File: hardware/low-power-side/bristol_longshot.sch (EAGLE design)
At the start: 68 parts, among them U1 SAM_D20E, U10 ADP1607ACPZN-R7, U11 TPS73118DBVT, U2 SI4060, U3 SE880, U4 SST25WF040BT-40I/NP, U5 TG-5006CJ, U6 TG-5006CJ, U7 TPS3123, U8 SN74LVC1G32DCKR, U9 MS5607-02BA03, Y1 ABS05

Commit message: [low-power-side] More work on board, vaguely complete. Added parts list
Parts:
- removed R10: 100kΩ, microbuilder_v3:RESISTOR_0402
- removed R11: 240kΩ, microbuilder_v3:RESISTOR_0402
- added R2, R3, R4: 10kΩ, microbuilder_v3:RESISTOR_0402
- C10: value 100nF -> 100pF
- C11: value 100nF -> 1nF
- C12: value 1µF -> 10nF
- C20: value 18pF -> 100nF
- C21: value 2.2µF -> 100nF
- C22: value 4.7µF -> 100nF
- C23: value 18pF -> 1µF
- C24: value 1nF -> 1µF
- C25: value 100nF -> 2.2µF
- C26: value 10µF -> 4.7µF; device resistor:C-EUC0603K -> microbuilder_v3:CAP_CERAMIC_0402
- C27, C28: value 10µF -> 18pF; device resistor:C-EUC0603K -> microbuilder_v3:CAP_CERAMIC_0402
- C29: value 1µF -> 10µF; device microbuilder_v3:CAP_CERAMIC_0402 -> resistor:C-EUC0603K
- C30: value 10nF -> 10µF; device microbuilder_v3:CAP_CERAMIC_0402 -> resistor:C-EUC0603K
- C31: value 100µF -> 10µF; device resistor:C-EUC1210K -> resistor:C-EUC0603K
- C32: value 100pF -> 100µF; device microbuilder_v3:CAP_CERAMIC_0402 -> resistor:C-EUC1210K
- R7, R9: value 10kΩ -> 100kΩ
- R8: value 10kΩ -> 43kΩ
- renumbered U$48 to A1
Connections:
- removed net GPS!RESET: U1.PA03
- new net EXT_THERMISTOR_SENSE: R7.2, U1.PA03
- net 1.2V: now also C29.1; no longer C27.1
- net 1.8V: now also C21.P$1, C26.P$1, C30.1, C32.1, R4.2, R8.2; no longer C22.P$1, C26.1, C31.1, C32.P$1, R10.2, R7.2
- net FB: now also R8.1, R9.2; no longer R10.1, R11.2
- net GND: now also C26.P$2, C27.P$2, C28.P$2, C29.2, C30.2, C32.2, R2.1, R3.1, R7.1; no longer C26.2, C27.2, C28.2, C29.P$2, C30.P$2, C32.P$2, R11.1, R8.1
- net RADIO_VDD: now also C20.P$1, C25.P$1; no longer C11.P$1, C21.P$1
- net RTC_XI: now also C27.P$1; no longer C20.P$1
- net RTC_XO: now also C28.P$1; no longer C23.P$1
- net SE_GPIO0: now also R2.2; no longer R9.2
- net SE_GPIO1: now also R3.2; no longer R8.2
- net SE_MODE_PULL: now also R4.1; no longer R7.1
- net TCXO_REG_IN: now also C23.P$1; no longer C29.P$1
- net TCXO_REG_NR: now also C12.P$1; no longer C30.P$1
- net TCXO_VDD: now also C24.P$1; no longer C12.P$1
- net TCXO_VDD1: now also C11.P$1, C22.P$1, C31.1; no longer C24.P$1, C25.P$1, C28.1
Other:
- note added: "Nominal output voltage 1.80V Using 0.1% resistors most of the variablity is in V_FB Specified 1.76V - 1.85V"
- note added: "Si4468 Transciever"
- note removed: "Si4060 Transmitter"
- moved on the sheet: C10, C11, C12, C20, C21, C22, C23, C24, C25, C26, C27, C28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

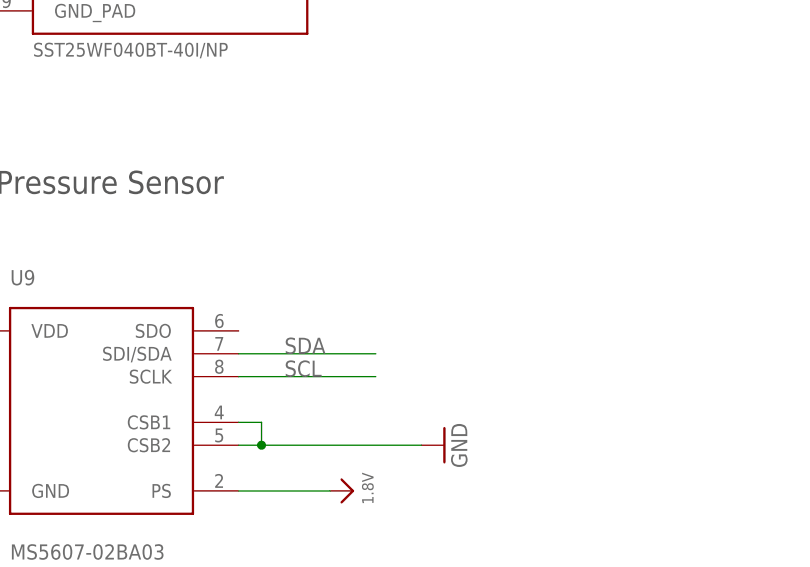
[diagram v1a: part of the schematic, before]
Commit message: [low-power-side] Added 10k i2c pull ups
v0.986.0 -> v0.986.1
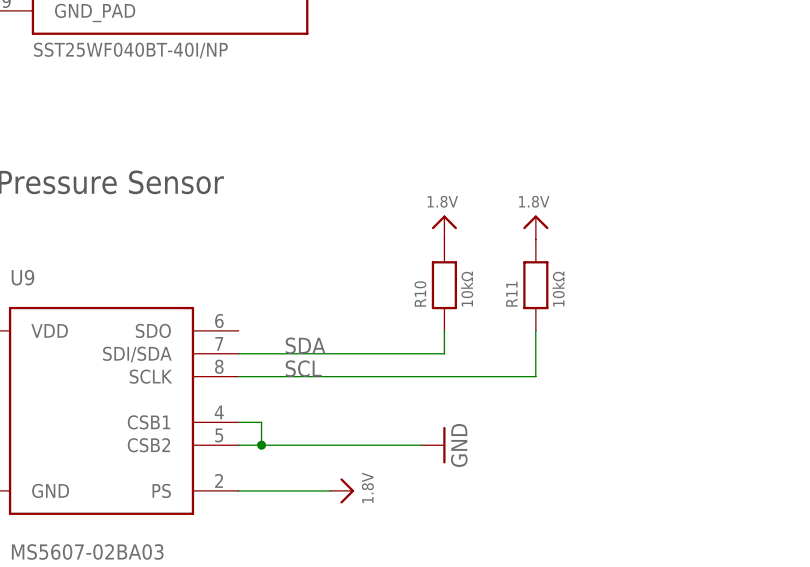
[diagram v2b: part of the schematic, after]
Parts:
- added R10, R11: 10kΩ, microbuilder_v3:RESISTOR_0402
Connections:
- net 1.8V: now also R10.2, R11.2
- net SCL: now also R11.1
- net SDA: now also R10.1
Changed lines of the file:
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@@
 <part name="U$47" library="microbuilder_v3" deviceset="GND" device=""/>
 <part name="U$53" library="microbuilder_v3" deviceset="1.8V" device=""/>
+<part name="R10" library="microbuilder_v3" deviceset="RESISTOR" device="_0402" value="10kΩ"/>
+<part name="R11" library="microbuilder_v3" deviceset="RESISTOR" device="_0402" value="10kΩ"/>
+<part name="U$48" library="microbuilder_v3" deviceset="1.8V" device=""/>
+<part name="U$54" library="microbuilder_v3" deviceset="1.8V" device=""/>
 </parts>
 <sheets>
@@
 <instance part="U$47" gate="G$1" x="40.64" y="119.38"/>
 <instance part="U$53" gate="G$1" x="40.64" y="147.32" rot="MR0"/>
+<instance part="R10" gate="G$1" x="256.54" y="45.72" rot="R90"/>
+<instance part="R11" gate="G$1" x="266.7" y="45.72" rot="R90"/>
+<instance part="U$48" gate="G$1" x="256.54" y="53.34" rot="MR0"/>
+<instance part="U$54" gate="G$1" x="266.7" y="53.34" rot="MR0"/>
 </instances>
 <busses>
@@
 <wire x1="40.64" y1="139.7" x2="5.08" y2="139.7" width="0.1524" layer="91"/>
 <label x="7.62" y="139.7" size="1.778" layer="95"/>
+</segment>
+<segment>
+<pinref part="R10" gate="G$1" pin="2"/>
+<pinref part="U$48" gate="G$1" pin="1.8V"/>
+</segment>
+<segment>
+<pinref part="R11" gate="G$1" pin="2"/>
+<pinref part="U$54" gate="G$1" pin="1.8V"/>
 </segment>
 </net>
@@
 <segment>
 <pinref part="U9" gate="A" pin="SDI/SDA"/>
-<wire x1="233.68" y1="38.1" x2="248.92" y2="38.1" width="0.1524" layer="91"/>
+<wire x1="233.68" y1="38.1" x2="256.54" y2="38.1" width="0.1524" layer="91"/>
 <label x="238.76" y="38.1" size="1.778" layer="95"/>
+<pinref part="R10" gate="G$1" pin="1"/>
+<wire x1="256.54" y1="38.1" x2="256.54" y2="40.64" width="0.1524" layer="91"/>
 </segment>
 </net>
@@
 <segment>
 <pinref part="U9" gate="A" pin="SCLK"/>
-<wire x1="233.68" y1="35.56" x2="248.92" y2="35.56" width="0.1524" layer="91"/>
 <label x="238.76" y="35.56" size="1.778" layer="95"/>
-</segment>
-</net>
+<pinref part="R11" gate="G$1" pin="1"/>
+<wire x1="233.68" y1="35.56" x2="266.7" y2="35.56" width="0.1524" layer="91"/>
+<wire x1="266.7" y1="35.56" x2="266.7" y2="40.64" width="0.1524" layer="91"/>
+</segment>
+</net>

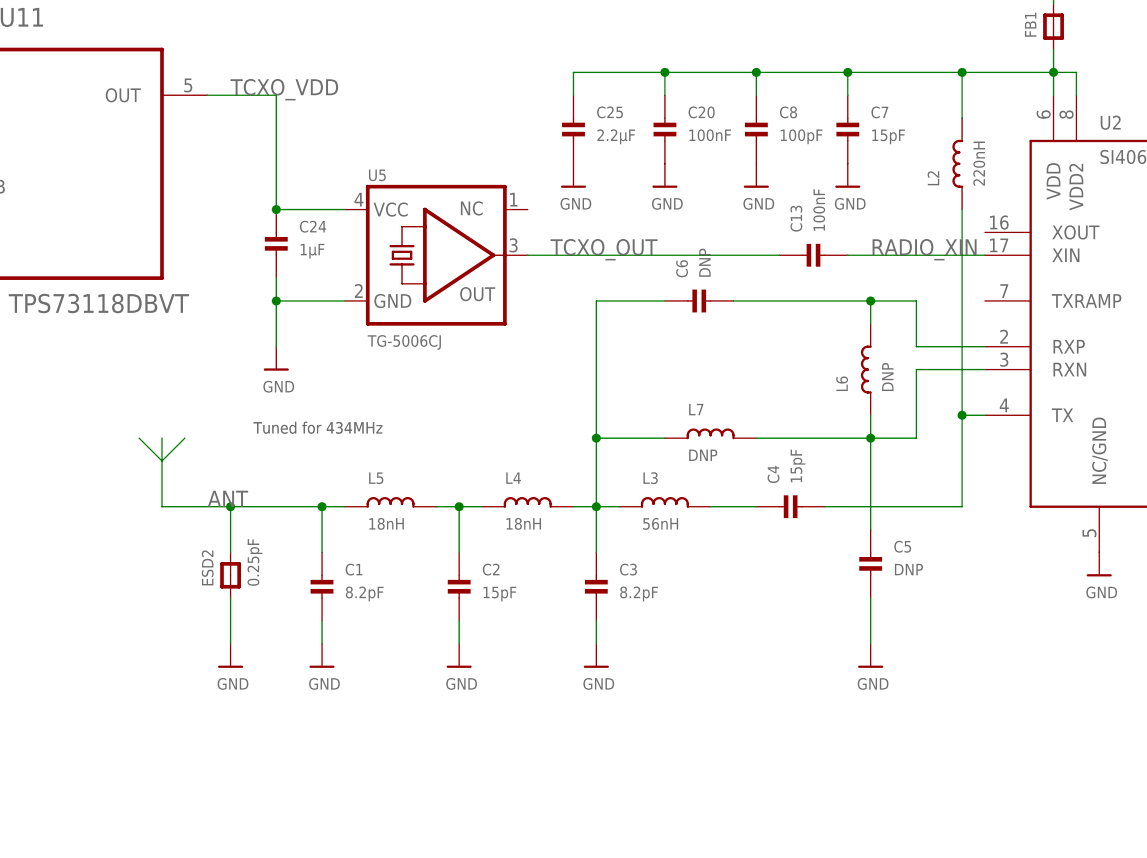
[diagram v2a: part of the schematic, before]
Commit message: [low-power] Rearranged matching section
Attempt to follow guidelines from silabs AN685 more closely
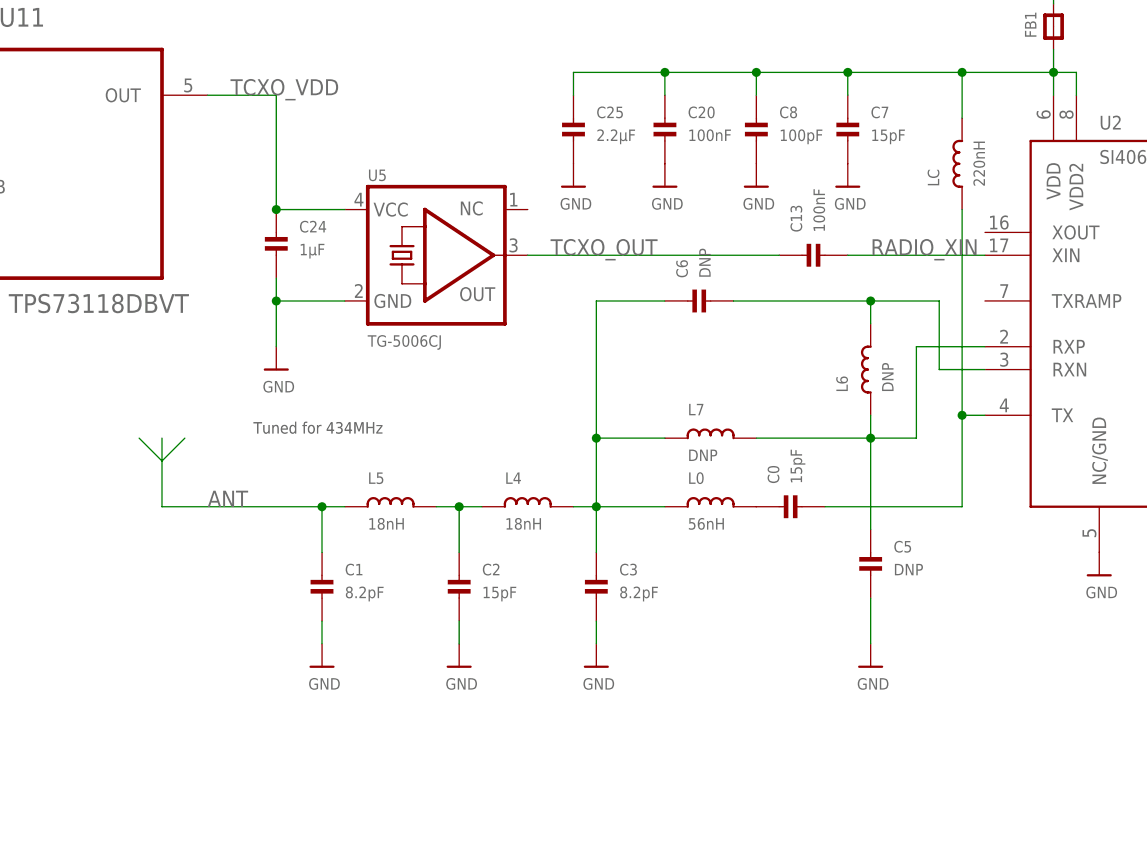
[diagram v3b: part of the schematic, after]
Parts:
- removed ESD2: 0.25pF, microbuilder_v3:FERRITE_0603MP
- removed L3: 56nH, microbuilder_v3:INDUCTOR_0402
- added L0: 56nH, microbuilder_v3:INDUCTOR_0402
- renumbered C4 to C0, L2 to LC
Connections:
- net ANT: no longer ESD2.P$2
- net FILTER1: now also L0.1; no longer L3.1
- net GND: no longer ESD2.P$1
- net RF_TANK: now also L0.2; no longer L3.2
- net RXN: now also U2.RXP; no longer U2.RXN
- net RXP: now also U2.RXN; no longer U2.RXP
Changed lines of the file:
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@@
 <part name="U$40" library="microbuilder_v3" deviceset="1.8V" device=""/>
 <part name="U$41" library="microbuilder_v3" deviceset="1.8V" device=""/>
-<part name="L2" library="microbuilder_v3" deviceset="INDUCTOR" device="_0402" value="220nH"/>
+<part name="LC" library="microbuilder_v3" deviceset="INDUCTOR" device="_0402" value="220nH"/>
 <part name="FB1" library="microbuilder_v3" deviceset="FERRITE" device="_0402"/>
-<part name="C4" library="microbuilder_v3" deviceset="CAP_CERAMIC" device="_0402" value="15pF"/>
-<part name="L3" library="microbuilder_v3" deviceset="INDUCTOR" device="_0402" value="56nH"/>
+<part name="C0" library="microbuilder_v3" deviceset="CAP_CERAMIC" device="_0402" value="15pF"/>
+<part name="L0" library="microbuilder_v3" deviceset="INDUCTOR" device="_0402" value="56nH"/>
 <part name="C3" library="microbuilder_v3" deviceset="CAP_CERAMIC" device="_0402" value="8.2pF"/>
 <part name="L4" library="microbuilder_v3" deviceset="INDUCTOR" device="_0402" value="18nH"/>
@@
 <part name="C13" library="microbuilder_v3" deviceset="CAP_CERAMIC" device="_0402" value="100nF"/>
 <part name="FB2" library="microbuilder_v3" deviceset="FERRITE" device="_0402"/>
-<part name="ESD2" library="microbuilder_v3" deviceset="FERRITE" device="_0603MP" value="0.25pF"/>
-<part name="U$31" library="microbuilder_v3" deviceset="GND" device=""/>
 <part name="U8" library="SN74LVC1G32DCKR" deviceset="SN74LVC1G32DCKR" device=""/>
 <part name="U$1" library="microbuilder_v3" deviceset="GND" device=""/>
@@
 <instance part="U$40" gate="G$1" x="185.42" y="96.52" rot="MR0"/>
 <instance part="U$41" gate="G$1" x="604.52" y="231.14" rot="MR0"/>
-<instance part="L2" gate="G$1" x="594.36" y="205.74" rot="R90"/>
+<instance part="LC" gate="G$1" x="594.36" y="205.74" rot="R90"/>
 <instance part="FB1" gate="G$1" x="604.52" y="220.98" rot="R90"/>
-<instance part="C4" gate="G$1" x="576.58" y="167.64" rot="R90"/>
-<instance part="L3" gate="G$1" x="561.34" y="167.64"/>
+<instance part="C0" gate="G$1" x="576.58" y="167.64" rot="R90"/>
+<instance part="L0" gate="G$1" x="566.42" y="167.64"/>
 <instance part="C3" gate="G$1" x="553.72" y="157.48"/>
 <instance part="L4" gate="G$1" x="546.1" y="167.64"/>
@@
 <instance part="C13" gate="G$1" x="579.12" y="195.58" rot="R90"/>
 <instance part="FB2" gate="G$1" x="454.66" y="223.52" rot="R90"/>
-<instance part="ESD2" gate="G$1" x="513.08" y="160.02" rot="R90"/>
-<instance part="U$31" gate="G$1" x="513.08" y="149.86"/>
 <instance part="U8" gate="A" x="99.06" y="203.2"/>
 <instance part="U$1" gate="G$1" x="78.74" y="177.8"/>
@@
 </segment>
 <segment>
-<pinref part="U$31" gate="G$1" pin="GND"/>
-<pinref part="ESD2" gate="G$1" pin="P$1"/>
-<wire x1="513.08" y1="152.4" x2="513.08" y2="157.48" width="0.1524" layer="91"/>
-</segment>
-<segment>
 <pinref part="U$1" gate="G$1" pin="GND"/>
 <wire x1="81.28" y1="193.04" x2="78.74" y2="193.04" width="0.1524" layer="91"/>
@@
 <wire x1="604.52" y1="215.9" x2="604.52" y2="218.44" width="0.1524" layer="91"/>
 <junction x="604.52" y="215.9"/>
-<pinref part="L2" gate="G$1" pin="2"/>
+<pinref part="LC" gate="G$1" pin="2"/>
 <wire x1="604.52" y1="215.9" x2="594.36" y2="215.9" width="0.1524" layer="91"/>
 <wire x1="594.36" y1="215.9" x2="594.36" y2="210.82" width="0.1524" layer="91"/>
@@
 <net name="RF_OUT" class="0">
 <segment>
-<pinref part="L2" gate="G$1" pin="1"/>
+<pinref part="LC" gate="G$1" pin="1"/>
 <wire x1="594.36" y1="200.66" x2="594.36" y2="177.8" width="0.1524" layer="91"/>
-<pinref part="C4" gate="G$1" pin="P$2"/>
+<pinref part="C0" gate="G$1" pin="P$2"/>
 <wire x1="594.36" y1="177.8" x2="594.36" y2="167.64" width="0.1524" layer="91"/>
 <wire x1="594.36" y1="167.64" x2="579.12" y2="167.64" width="0.1524" layer="91"/>
@@
 <net name="FILTER1" class="0">
 <segment>
-<pinref part="L3" gate="G$1" pin="1"/>
+<pinref part="L0" gate="G$1" pin="1"/>
 <pinref part="L4" gate="G$1" pin="2"/>
-<wire x1="556.26" y1="167.64" x2="553.72" y2="167.64" width="0.1524" layer="91"/>
+<wire x1="561.34" y1="167.64" x2="553.72" y2="167.64" width="0.1524" layer="91"/>
 <pinref part="C3" gate="G$1" pin="P$1"/>
 <wire x1="553.72" y1="167.64" x2="551.18" y2="167.64" width="0.1524" layer="91"/>
@@
 <wire x1="525.78" y1="167.64" x2="523.24" y2="167.64" width="0.1524" layer="91"/>
 <wire x1="523.24" y1="167.64" x2="523.24" y2="162.56" width="0.1524" layer="91"/>
-<wire x1="505.46" y1="167.64" x2="513.08" y2="167.64" width="0.1524" layer="91"/>
 <label x="510.54" y="167.64" size="1.778" layer="95" ratio="11"/>
 <junction x="523.24" y="167.64"/>
-<wire x1="513.08" y1="167.64" x2="523.24" y2="167.64" width="0.1524" layer="91"/>
+<wire x1="505.46" y1="167.64" x2="523.24" y2="167.64" width="0.1524" layer="91"/>
 <wire x1="505.46" y1="167.64" x2="505.46" y2="172.72" width="0.1524" layer="91"/>
 <wire x1="505.46" y1="175.26" x2="505.46" y2="172.72" width="0.1524" layer="91"/>
 <wire x1="502.92" y1="175.26" x2="505.46" y2="172.72" width="0.1524" layer="91"/>
 <wire x1="505.46" y1="172.72" x2="508" y2="175.26" width="0.1524" layer="91"/>
-<pinref part="ESD2" gate="G$1" pin="P$2"/>
-<wire x1="513.08" y1="162.56" x2="513.08" y2="167.64" width="0.1524" layer="91"/>
-<junction x="513.08" y="167.64"/>
 </segment>
 </net>
 <net name="RXP" class="0">
 <segment>
-<pinref part="U2" gate="G$1" pin="RXP"/>
-<wire x1="596.9" y1="185.42" x2="589.28" y2="185.42" width="0.1524" layer="91"/>
-<wire x1="589.28" y1="185.42" x2="589.28" y2="190.5" width="0.1524" layer="91"/>
+<wire x1="591.82" y1="182.88" x2="591.82" y2="190.5" width="0.1524" layer="91"/>
 <pinref part="L6" gate="G$1" pin="2"/>
-<wire x1="589.28" y1="190.5" x2="584.2" y2="190.5" width="0.1524" layer="91"/>
+<wire x1="591.82" y1="190.5" x2="584.2" y2="190.5" width="0.1524" layer="91"/>
 <wire x1="584.2" y1="190.5" x2="584.2" y2="187.96" width="0.1524" layer="91"/>
 <pinref part="C6" gate="G$1" pin="P$2"/>
 <wire x1="568.96" y1="190.5" x2="584.2" y2="190.5" width="0.1524" layer="91"/>
 <junction x="584.2" y="190.5"/>
+<pinref part="U2" gate="G$1" pin="RXN"/>
+<wire x1="591.82" y1="182.88" x2="596.9" y2="182.88" width="0.1524" layer="91"/>
 </segment>
 </net>
 <net name="RXN" class="0">
 <segment>
-<pinref part="U2" gate="G$1" pin="RXN"/>
-<wire x1="596.9" y1="182.88" x2="589.28" y2="182.88" width="0.1524" layer="91"/>
-<wire x1="589.28" y1="182.88" x2="589.28" y2="175.26" width="0.1524" layer="91"/>
+<wire x1="589.28" y1="185.42" x2="589.28" y2="175.26" width="0.1524" layer="91"/>
 <pinref part="L6" gate="G$1" pin="1"/>
 <wire x1="589.28" y1="175.26" x2="584.2" y2="175.26" width="0.1524" layer="91"/>
@@
 <pinref part="C5" gate="G$1" pin="P$1"/>
 <wire x1="584.2" y1="175.26" x2="584.2" y2="165.1" width="0.1524" layer="91"/>
+<pinref part="U2" gate="G$1" pin="RXP"/>
+<wire x1="596.9" y1="185.42" x2="589.28" y2="185.42" width="0.1524" layer="91"/>
 </segment>
 </net>
@@
 <net name="RF_TANK" class="0">
 <segment>
-<pinref part="C4" gate="G$1" pin="P$1"/>
-<pinref part="L3" gate="G$1" pin="2"/>
-<wire x1="571.5" y1="167.64" x2="566.42" y2="167.64" width="0.1524" layer="91"/>
-</segment>
-</net>
+<pinref part="C0" gate="G$1" pin="P$1"/>
+<pinref part="L0" gate="G$1" pin="2"/>
+</segment>
+</net>
